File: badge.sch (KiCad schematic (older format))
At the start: 40 parts, among them J1 DevKitC_L, J10 IR333C, J11 DUST, J12 DevKitC_L_SMD, J13 DevKitC_R_SMD, J14 220uF, J2 DevKitC_R, J3 HT024SQV010NH, J4 ADC_3, J5 ADC_2, J6 ADC_1, J7 DAC_1, J8 DAC_2, J9 HSPI, Q1 2N7002, SW3 A, SW6 B, SW7 SW_DIP_x03, U1 ESP32-DEVKITC-32D

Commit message: Update v0.4, vertical long before tracks
* Move footprint library to DeveloperDay2018Badge
* Add symbol library, 3D models into project
* Change board color
* Increase R, C, LED size to 0805(2012)
* Remove front solder mask for ESP32 DevKitC socket header, to make clean SMD socket pad.
* Add silk for ESP32 DevKitC
* Add silk direction in footprint for ITS-1550S-B 5 way tact switch
* Add footprint and 3D for ITS-1106 tact switch
* Change ESP32 DevKitC 3D model from SnapEDA
* Remove THT 19pin socket 3D for ESP32 DevKitC
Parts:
- C2, C3: value 0603/0.1uF -> 2012/0.1uF; footprint Capacitor_SMD:C_0603_1608Metric -> Capacitor_SMD:C_0805_2012Metric
- C8: value 0.1uF -> 2012/0.1uF; footprint Capacitor_SMD:C_0603_1608Metric -> Capacitor_SMD:C_0805_2012Metric
- D1: value 0603/BLUE -> 2012/BLUE; footprint LED_SMD:LED_0603_1608Metric -> LED_SMD:LED_0805_2012Metric
- D2: value 0603/RED -> 2012/RED; footprint LED_SMD:LED_0603_1608Metric -> LED_SMD:LED_0805_2012Metric
- J1, J2: footprint Connector_PinSocket_2.54mm:PinSocket_1x19_P2.54mm_Vertical -> DeveloperDay2018Badge:PinSocket_1x19_P2.54mm_Vertical_BackOnly_NO3D
- J10, J14: footprint custom_footprint:PinSocket_1x02_P2.54mm_Vertical_NO3D -> DeveloperDay2018Badge:PinSocket_1x02_P2.54mm_Vertical_NO3D
- LCD1: footprint custom_footprint:2.4INCH_TFT_LCD_18P_0.80mm_FOLD -> DeveloperDay2018Badge:2.4INCH_TFT_LCD_18P_0.80mm_FOLD_JGKONG
- R4: value 0603/4.7R -> 2012/4.7R; footprint Resistor_SMD:R_0603_1608Metric -> Resistor_SMD:R_0805_2012Metric
- R5: value 0603/470R -> 2012/470R; footprint Resistor_SMD:R_0603_1608Metric -> Resistor_SMD:R_0805_2012Metric
- R6: value 0603/1K -> 2012/1K; footprint Resistor_SMD:R_0603_1608Metric -> Resistor_SMD:R_0805_2012Metric
- R7: value 0603/220R -> 2012/220R; footprint Resistor_SMD:R_0603_1608Metric -> Resistor_SMD:R_0805_2012Metric
- R8: value 0603/20R -> 2012/20R; footprint Resistor_SMD:R_0603_1608Metric -> Resistor_SMD:R_0805_2012Metric
- R9: value 0603/36R -> 2012/36R; footprint Resistor_SMD:R_0603_1608Metric -> Resistor_SMD:R_0805_2012Metric
- SW3, SW6: footprint Button_Switch_SMD:SW_SPST_TL3342 -> DeveloperDay2018Badge:ITS-1106S
- SW7: value SW_DIP_x03 -> ITS_1500S_B; footprint custom_footprint:ITS-1500S-A -> DeveloperDay2018Badge:ITS-1500S-B-SILKDIR
- U1: footprint custom_footprint:MODULE_ESP32-DEVKITC-32D-SILKONLY -> DeveloperDay2018Badge:MODULE_ESP32-DEVKITC-32D-SILKONLY-SIMPLE
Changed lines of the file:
@@
 F 0 "U1" H 3000 3167 50  0000 C CNN
 F 1 "ESP32-DEVKITC-32D" H 3000 3076 50  0000 C CNN
-F 2 "custom_footprint:MODULE_ESP32-DEVKITC-32D-SILKONLY" H 3000 2000 50  0001 L BNN
+F 2 "DeveloperDay2018Badge:MODULE_ESP32-DEVKITC-32D-SILKONLY-SIMPLE" H 3000 2000 50  0001 L BNN
 F 3 "None" H 3000 2000 50  0001 L BNN
 F 4 "Espressif Systems" H 3000 2000 50  0001 L BNN "Field4"
@@
 F 0 "J1" H 2000 3100 50  0000 L CNN
 F 1 "DevKitC_L" H 1800 3000 50  0000 L CNN
-F 2 "Connector_PinSocket_2.54mm:PinSocket_1x19_P2.54mm_Vertical" H 2100 2000 50  0001 C CNN
+F 2 "DeveloperDay2018Badge:PinSocket_1x19_P2.54mm_Vertical_BackOnly_NO3D" H 2100 2000 50  0001 C CNN
 F 3 "~" H 2100 2000 50  0001 C CNN
 	1    2100 2000
@@
 F 0 "J2" H 3794 3085 50  0000 C CNN
 F 1 "DevKitC_R" H 3794 2994 50  0000 C CNN
-F 2 "Connector_PinSocket_2.54mm:PinSocket_1x19_P2.54mm_Vertical" H 3900 2000 50  0001 C CNN
+F 2 "DeveloperDay2018Badge:PinSocket_1x19_P2.54mm_Vertical_BackOnly_NO3D" H 3900 2000 50  0001 C CNN
 F 3 "~" H 3900 2000 50  0001 C CNN
 	1    3900 2000
@@
 F 0 "SW3" H 4700 7200 50  0000 C CNN
 F 1 "A" H 5100 7200 50  0000 C CNN
-F 2 "Button_Switch_SMD:SW_SPST_TL3342" H 4900 7300 50  0001 C CNN
+F 2 "DeveloperDay2018Badge:ITS-1106S" H 4900 7300 50  0001 C CNN
 F 3 "" H 4900 7300 50  0001 C CNN
 	1    4900 7100
@@
 F 0 "SW6" H 4700 7500 50  0000 C CNN
 F 1 "B" H 5100 7500 50  0000 C CNN
-F 2 "Button_Switch_SMD:SW_SPST_TL3342" H 4900 7600 50  0001 C CNN
+F 2 "DeveloperDay2018Badge:ITS-1106S" H 4900 7600 50  0001 C CNN
 F 3 "" H 4900 7600 50  0001 C CNN
 	1    4900 7400
@@
 P 6300 1900
 F 0 "C8" H 6150 1950 50  0000 L CNN
-F 1 "0.1uF" H 6050 1800 50  0000 L CNN
-F 2 "Capacitor_SMD:C_0603_1608Metric" H 6300 1900 50  0001 C CNN
+F 1 "2012/0.1uF" H 6050 1800 50  0000 L CNN
+F 2 "Capacitor_SMD:C_0805_2012Metric" H 6300 1900 50  0001 C CNN
 F 3 "~" H 6300 1900 50  0001 C CNN
 	1    6300 1900
@@
 P 6600 2500
 F 0 "R4" H 6500 2500 50  0000 C CNN
-F 1 "0603/4.7R" H 6200 2500 50  0000 C CNN
-F 2 "Resistor_SMD:R_0603_1608Metric" H 6600 2500 50  0001 C CNN
+F 1 "2012/4.7R" H 6200 2500 50  0000 C CNN
+F 2 "Resistor_SMD:R_0805_2012Metric" H 6600 2500 50  0001 C CNN
 F 3 "~" H 6600 2500 50  0001 C CNN
 	1    6600 2500
@@
 F 0 "LCD1" H 10553 5384 50  0000 L CNN
 F 1 "2.4\" LCD" H 10553 5293 50  0000 L CNN
-F 2 "custom_footprint:2.4INCH_TFT_LCD_18P_0.80mm_FOLD" H 10450 5400 50  0001 C CNN
+F 2 "DeveloperDay2018Badge:2.4INCH_TFT_LCD_18P_0.80mm_FOLD_JGKONG" H 10450 5400 50  0001 C CNN
 F 3 "~" H 10450 5400 50  0001 C CNN
 	1    10400 5350
@@
 P 7300 5750
 F 0 "D1" H 7291 5966 50  0000 C CNN
-F 1 "0603/BLUE" H 7291 5875 50  0000 C CNN
-F 2 "LED_SMD:LED_0603_1608Metric" H 7300 5750 50  0001 C CNN
+F 1 "2012/BLUE" H 7291 5875 50  0000 C CNN
+F 2 "LED_SMD:LED_0805_2012Metric" H 7300 5750 50  0001 C CNN
 F 3 "~" H 7300 5750 50  0001 C CNN
 	1    7300 5750
@@
 P 7800 5750
 F 0 "R5" V 7593 5750 50  0000 C CNN
-F 1 "0603/470R" V 7684 5750 50  0000 C CNN
-F 2 "Resistor_SMD:R_0603_1608Metric" V 7730 5750 50  0001 C CNN
+F 1 "2012/470R" V 7684 5750 50  0000 C CNN
+F 2 "Resistor_SMD:R_0805_2012Metric" V 7730 5750 50  0001 C CNN
 F 3 "~" H 7800 5750 50  0001 C CNN
 	1    7800 5750
@@
 P 7300 6100
 F 0 "D2" H 7291 6316 50  0000 C CNN
-F 1 "0603/RED" H 7291 6225 50  0000 C CNN
-F 2 "LED_SMD:LED_0603_1608Metric" H 7300 6100 50  0001 C CNN
+F 1 "2012/RED" H 7291 6225 50  0000 C CNN
+F 2 "LED_SMD:LED_0805_2012Metric" H 7300 6100 50  0001 C CNN
 F 3 "~" H 7300 6100 50  0001 C CNN
 	1    7300 6100
@@
 P 7800 6100
 F 0 "R6" V 7593 6100 50  0000 C CNN
-F 1 "0603/1K" V 7684 6100 50  0000 C CNN
-F 2 "Resistor_SMD:R_0603_1608Metric" V 7730 6100 50  0001 C CNN
+F 1 "2012/1K" V 7684 6100 50  0000 C CNN
+F 2 "Resistor_SMD:R_0805_2012Metric" V 7730 6100 50  0001 C CNN
 F 3 "~" H 7800 6100 50  0001 C CNN
 	1    7800 6100
@@
 P 9000 5600
 F 0 "R7" V 8900 5700 50  0000 C CNN
-F 1 "0603/220R" V 8900 5400 50  0000 C CNN
-F 2 "Resistor_SMD:R_0603_1608Metric" H 9000 5600 50  0001 C CNN
+F 1 "2012/220R" V 8900 5400 50  0000 C CNN
+F 2 "Resistor_SMD:R_0805_2012Metric" H 9000 5600 50  0001 C CNN
 F 3 "~" H 9000 5600 50  0001 C CNN
 	1    9000 5600
@@
 P 4900 6800
 F 0 "SW7" H 4900 7267 50  0000 C CNN
-F 1 "SW_DIP_x03" H 4900 7176 50  0000 C CNN
-F 2 "custom_footprint:ITS-1500S-A" H 4900 6800 50  0001 C CNN
+F 1 "ITS_1500S_B" H 4900 7176 50  0000 C CNN
+F 2 "DeveloperDay2018Badge:ITS-1500S-B-SILKDIR" H 4900 6800 50  0001 C CNN
 F 3 "" H 4900 6800 50  0001 C CNN
 	1    4900 6800
@@
 F 0 "J14" V 8900 5900 50  0000 R CNN
 F 1 "220uF" V 8800 6000 50  0000 R CNN
-F 2 "custom_footprint:PinSocket_1x02_P2.54mm_Vertical_NO3D" H 8900 5700 50  0001 C CNN
+F 2 "DeveloperDay2018Badge:PinSocket_1x02_P2.54mm_Vertical_NO3D" H 8900 5700 50  0001 C CNN
 F 3 "~" H 8900 5700 50  0001 C CNN
 	1    8900 5700
@@
 P 3400 5800
 F 0 "C2" V 3300 5800 50  0000 C CNN
-F 1 "0603/0.1uF" V 3300 6100 50  0000 C CNN
-F 2 "Capacitor_SMD:C_0603_1608Metric" H 3400 5800 50  0001 C CNN
+F 1 "2012/0.1uF" V 3300 6100 50  0000 C CNN
+F 2 "Capacitor_SMD:C_0805_2012Metric" H 3400 5800 50  0001 C CNN
 F 3 "~" H 3400 5800 50  0001 C CNN
 	1    3400 5800
@@
 P 3400 6100
 F 0 "C3" V 3500 6100 50  0000 C CNN
-F 1 "0603/0.1uF" V 3500 6400 50  0000 C CNN
-F 2 "Capacitor_SMD:C_0603_1608Metric" H 3400 6100 50  0001 C CNN
+F 1 "2012/0.1uF" V 3500 6400 50  0000 C CNN
+F 2 "Capacitor_SMD:C_0805_2012Metric" H 3400 6100 50  0001 C CNN
 F 3 "~" H 3400 6100 50  0001 C CNN
 	1    3400 6100
@@
 P 7300 4900
 F 0 "R8" V 7400 5000 50  0000 C CNN
-F 1 "0603/20R" V 7400 4700 50  0000 C CNN
-F 2 "Resistor_SMD:R_0603_1608Metric" H 7300 4900 50  0001 C CNN
+F 1 "2012/20R" V 7400 4700 50  0000 C CNN
+F 2 "Resistor_SMD:R_0805_2012Metric" H 7300 4900 50  0001 C CNN
 F 3 "~" H 7300 4900 50  0001 C CNN
 	1    7300 4900
@@
 P 7700 4600
 F 0 "R9" H 7800 4600 50  0000 C CNN
-F 1 "0603/36R" H 8100 4600 50  0000 C CNN
-F 2 "Resistor_SMD:R_0603_1608Metric" H 7700 4600 50  0001 C CNN
+F 1 "2012/36R" H 8100 4600 50  0000 C CNN
+F 2 "Resistor_SMD:R_0805_2012Metric" H 7700 4600 50  0001 C CNN
 F 3 "~" H 7700 4600 50  0001 C CNN
 	1    7700 4600
@@
 F 0 "J10" H 8100 4500 50  0000 R CNN
 F 1 "IR333C" H 8200 4600 50  0000 R CNN
-F 2 "custom_footprint:PinSocket_1x02_P2.54mm_Vertical_NO3D" H 7900 4500 50  0001 C CNN
+F 2 "DeveloperDay2018Badge:PinSocket_1x02_P2.54mm_Vertical_NO3D" H 7900 4500 50  0001 C CNN
 F 3 "~" H 7900 4500 50  0001 C CNN
 	1    7900 4500
@@
 	8200 4100 6700 4100
 $Comp
-L power:+5V #PWR?
+L power:+5V #PWR0123
 U 1 1 5BDC3EDC
 P 7700 4400
-F 0 "#PWR?" H 7700 4250 50  0001 C CNN
+F 0 "#PWR0123" H 7700 4250 50  0001 C CNN
 F 1 "+5V" H 7715 4573 50  0000 C CNN
 F 2 "" H 7700 4400 50  0001 C CNN

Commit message: Rout'ing
* Add dummy pad for ESP32 DevKitC footprint to avoid errors
* Add silk guide for LCD attachment
* Add alternative 40pin LCD connector
* Add logo and information in silk layer
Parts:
- removed C1: 0.1uF, Capacitor_SMD:C_0603_1608Metric, symbol Device:C_Small
- removed R1, R2, R3: 0603/10R, Resistor_SMD:R_0603_1608Metric, symbol Device:R_Small
- added LCD2: 2.4\" LCD 40PIN, DeveloperDay2018Badge:2.4INCH_TFT_LCD_40P_0.50mm_FOLD, symbol Mechanical:Housing
- D1, D2: symbol Device:LED -> Device:LED_Small
- DS1: value EZ240IT010 -> 18PIN LCD; symbol New_Library:LCD_SPI_18P -> DeveloperDay2018_Library:LCD_SPI_18P
- DS2: renamed from J3; value HT024SQV010NH -> 40PIN LCD; symbol New_Library:HT024SQV010NH -> DeveloperDay2018_Library:HT024SQV010NH
- LCD1: value 2.4\" LCD -> 2.4\" LCD 18PIN
- R5, R6: symbol Device:R -> Device:R_Small
- U1: symbol ESP32-DEVKITC-32D:ESP32-DEVKITC-32D -> DeveloperDay2018_Library:ESP32-DEVKITC-32D
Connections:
- net GND: now also D1.1 (K), D2.1 (K), DS2.17 (DB0), DS2.18 (DB1), DS2.19 (DB2), DS2.20 (DB3), DS2.21 (DB4), DS2.22 (DB5), DS2.23 (DB6), DS2.24 (DB7), DS2.25 (DB8), DS2.26 (DB9), DS2.27 (DB10), DS2.28 (DB11), DS2.29 (DB12), DS2.30 (DB13), DS2.31 (DB14), DS2.32 (DB15), DS2.34 (LED-K), DS2.35 (LED-K), DS2.36 (LED-K); no longer R5.1, R6.1
- net GPIO12: now also SW7.3; no longer SW7.1
- net GPIO14: now also SW7.5; no longer SW7.3
- net GPIO15: now also SW7.1; no longer SW7.5
- net GPIO16: now also R5.2, R8.2; no longer D1.2 (A)
- net GPIO17: now also R6.2; no longer D2.2 (A)
- net GPIO27: no longer R8.2
- net GPIO32: now also SW7.6
- net GPIO36: now also C3.2, J5.4 (Pin_4); no longer C2.2, J5.3 (Pin_3)
- net GPIO39: now also C2.2, J5.3 (Pin_3); no longer C3.2, J5.4 (Pin_4), SW7.6
- net LCD_DC: now also DS2.11 (/WR(DC)); no longer DS2.10 (RS)
- net VSPI_SCK: now also DS2.10 (RS(SCK)); no longer DS2.11 (/WR)
- new net: D1.2 (A), R5.1
- new net: D2.2 (A), R6.1
- no-connect marks 83 -> 67
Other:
- note removed: "IR LED\n"
- note removed: "NOT FOR USE"
- moved on the sheet: C2, C3, C8, D1, D2, DS1, H1, H2, H5, H6, J10, J11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

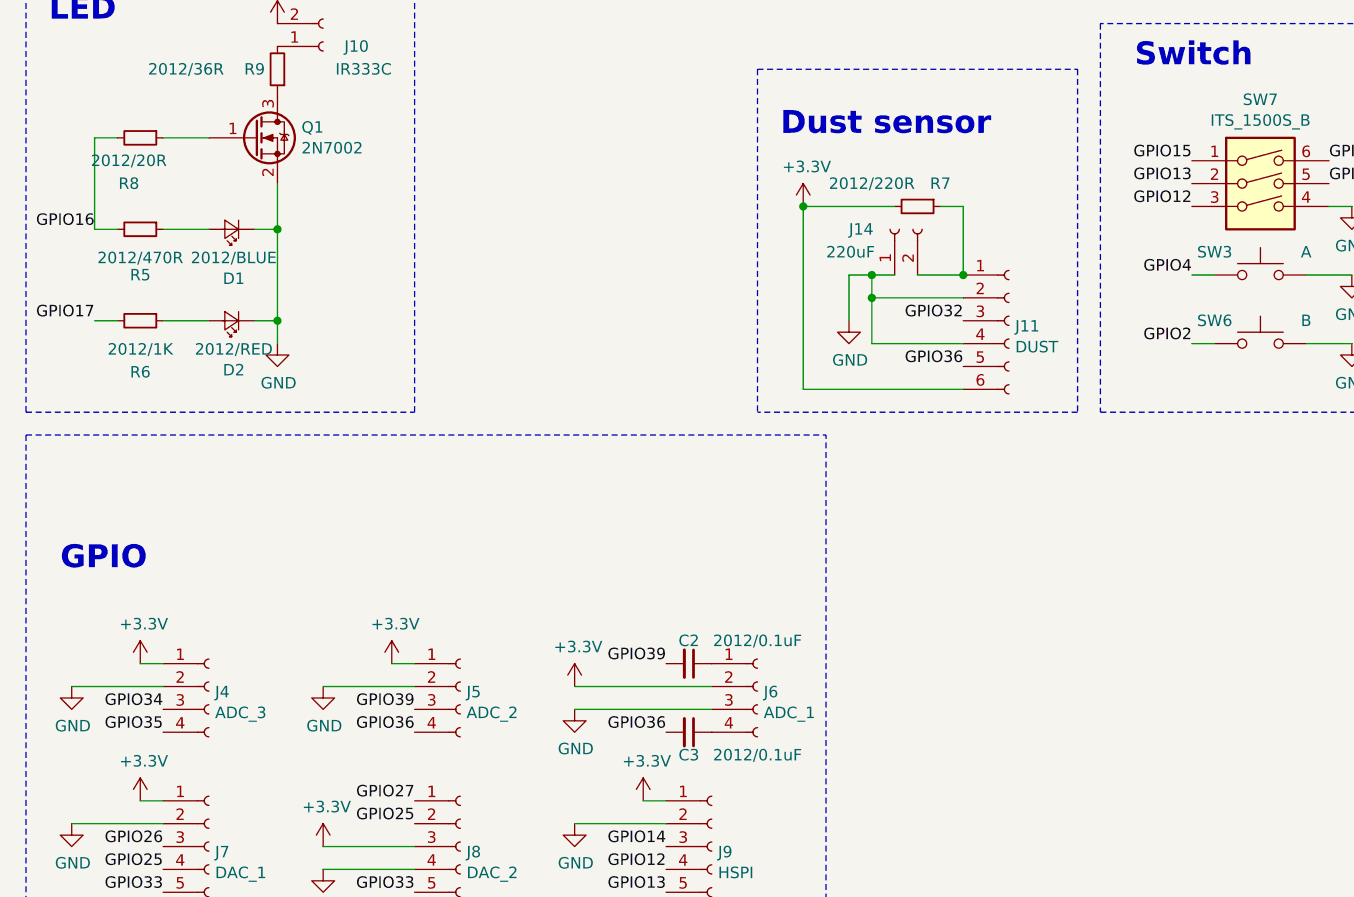
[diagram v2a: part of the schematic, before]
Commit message: v0.5 Finish tracks, final review
* Remove paste at 18pin LCD
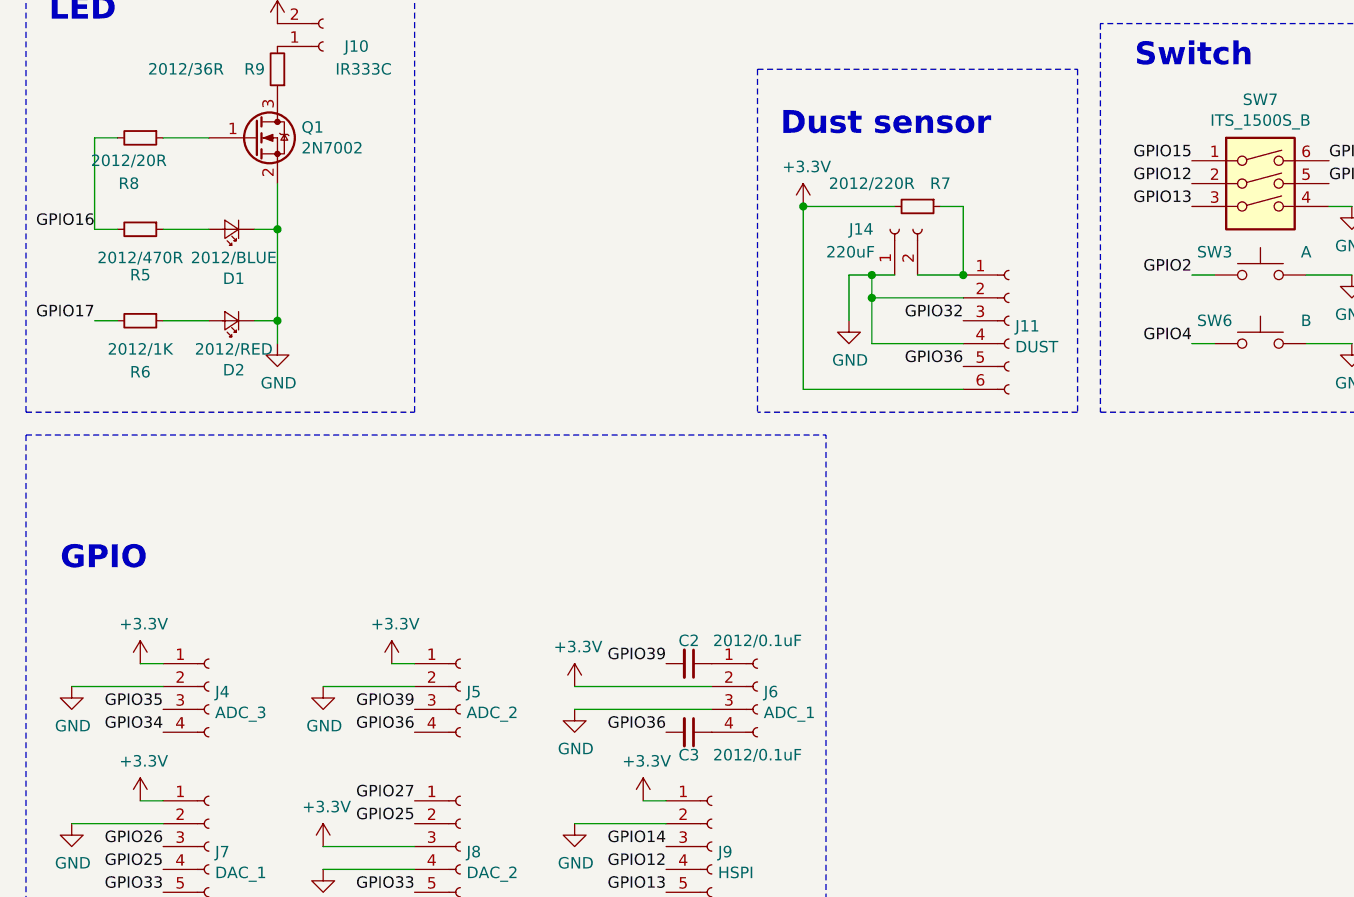
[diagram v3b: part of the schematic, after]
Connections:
- net GPIO12: now also SW7.2; no longer SW7.3
- net GPIO13: now also SW7.3; no longer SW7.2
- net GPIO2: now also SW3.1; no longer SW6.1
- net GPIO34: now also J4.4 (Pin_4); no longer J4.3 (Pin_3)
- net GPIO35: now also J4.3 (Pin_3); no longer J4.4 (Pin_4)
- net GPIO4: now also SW6.1; no longer SW3.1
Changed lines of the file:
@@
 	1    0    0    -1
 $EndComp
+Text Label 1100 6800 2    50   ~ 0
+GPIO34
+Wire Wire Line
+	700  6600 1100 6600
 Text Label 1100 6700 2    50   ~ 0
-GPIO34
-Wire Wire Line
-	700  6600 1100 6600
-Text Label 1100 6800 2    50   ~ 0
 GPIO35
 Text Label 1900 1600 2    50   ~ 0
@@
 	1    0    0    -1
 $EndComp
-Text Label 5600 4800 2    50   ~ 0
+Text Label 5600 5100 2    50   ~ 0
 GPIO4
 Wire Wire Line
@@
 	1    0    0    -1
 $EndComp
-Text Label 5600 5100 2    50   ~ 0
+Text Label 5600 4800 2    50   ~ 0
 GPIO2
 Wire Wire Line
@@
 Wire Wire Line
 	6200 4500 6300 4500
+Text Label 5600 4400 2    50   ~ 0
+GPIO12
 Text Label 5600 4500 2    50   ~ 0
-GPIO12
-Text Label 5600 4400 2    50   ~ 0
 GPIO13
 Text Label 6200 4400 0    50   ~ 0

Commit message: v1.0 release
* Update 40pin footprint
* Update tracks
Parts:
- DS1: footprint custom_footprint:COMMON_MOUNT_FFC-1x18-1MP_P0.80mm -> DeveloperDay2018Badge:COMMON_MOUNT_FFC-1x18-1MP_P0.80mm
- DS2: footprint Connector_FFC-FPC:Hirose_FH12-40S-0.5SH_1x40-1MP_P0.50mm_Horizontal -> DeveloperDay2018Badge:Yeonho_05002HR-40C_1x40-1MP_P0.50mm_Horizontal
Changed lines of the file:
@@
 F 0 "DS1" H 8500 3000 50  0000 L CNN
 F 1 "18PIN LCD" H 8200 1000 50  0000 L CNN
-F 2 "custom_footprint:COMMON_MOUNT_FFC-1x18-1MP_P0.80mm" H 8450 2100 50  0001 C CNN
+F 2 "DeveloperDay2018Badge:COMMON_MOUNT_FFC-1x18-1MP_P0.80mm" H 8450 2100 50  0001 C CNN
 F 3 "" H 8450 2100 50  0001 C CNN
 	1    8500 2100
@@
 F 0 "DS2" H 9000 -1400 50  0000 L CNN
 F 1 "40PIN LCD" H 9000 -1500 50  0000 L CNN
-F 2 "Connector_FFC-FPC:Hirose_FH12-40S-0.5SH_1x40-1MP_P0.50mm_Horizontal" H 9800 700 50  0001 C CNN
+F 2 "DeveloperDay2018Badge:Yeonho_05002HR-40C_1x40-1MP_P0.50mm_Horizontal" H 9800 700 50  0001 C CNN
 F 3 "" H 9800 700 50  0001 C CNN
 	1    9800 700

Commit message: Fix 3D model path into project
* Change R values
* Fix a few tracks
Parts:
- D2: value 2012/RED -> 2012/YELLOW
- H1, H2, H5, H6: footprint custom_footprint:LanyardHole_6mm -> DeveloperDay2018Badge:LanyardHole_6mm
- J1: footprint DeveloperDay2018Badge:PinSocket_1x19_P2.54mm_Vertical_BackOnly_NO3D -> DeveloperDay2018Badge:PinSocket_1x19_P2.54mm_Vertical_Universal_Pin1Right
- Q1: value 2N7002 -> SOT23/2N7002
- R5: value 2012/470R -> 2012/1K
- R8: value 2012/20R -> 2012/4.7R
- R9: value 2012/36R -> 2012/4.7R
- SW3, SW6: footprint DeveloperDay2018Badge:ITS-1106S -> DeveloperDay2018Badge:ITS-1103S
